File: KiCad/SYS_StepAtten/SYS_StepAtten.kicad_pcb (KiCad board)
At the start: 2 copper layers, 122 x 84 mm, 147 parts, among them J1 RCA-Out, J10 RCA1 GND JMP, J11 RCA2 GND JMP, J2 RCA-1, J3 RCA-2, J4 AUX-1-2, J5 Barrel_Jack 9Vac, J6 POT_EXT Conn, J7 cfg jumper, J8 ARM SWD, J9 A/D GND Jumper, K1 TQ2SA, K10 TQ2SA, K11 TQ2SA, K12 TQ2SA, K13 TQ2SA, K14 TQ2SA, K2 TQ2SA, K3 TQ2SA, K4 TQ2SA, K5 TQ2SA, K6 TQ2SA, K7 TQ2SA, K8 TQ2SA, K9 TQ2SA, Q1 2N7002, Q10 2N7002, Q11 2N7002, Q12 2N7002, Q13 2N7002, Q14 2N7002, Q2 2N7002, Q3 2N7002, Q4 2N7002, Q5 2N7002, Q6 2N7002, Q7 2N7002, Q8 2N7002, Q9 2N7002, SW1 INPUT_SWITCH, SW2 ON/OFF, U1 LM317, U2 L7805, U3 L7805, U4 STM32f030K6T6, Y1 8Mhz

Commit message: Base without relays
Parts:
- removed C6, C7: 22pf, Capacitor_SMD:C_0603_1608Metric
- removed Y1: 8Mhz, Crystal:Crystal_SMD_EuroQuartz_MJ-4Pin_5.0x3.2mm
- J10, J11: footprint Connector_PinSocket_2.54mm:PinSocket_1x03_P2.54mm_Vertical -> Connector_PinHeader_2.54mm:PinHeader_1x03_P2.54mm_Vertical
- moved Q14 440.9 mm to (642.0, -72.4)
- moved D23 424.9 mm to (647.1, -73.0), turned to 180 degrees
- moved Q13 416.0 mm to (624.2, -87.6)
- moved D22 402.5 mm to (629.2, -83.8), turned to 180 degrees
- moved Q12 358.2 mm to (561.3, -73.0)
- moved D21 340.3 mm to (566.4, -70.5)
- moved Q11 330.7 mm to (546.7, -73.7)
- moved D20 325.8 mm to (549.9, -64.1)
- moved Q10 297.6 mm to (518.8, -78.1)
- moved D19 289.7 mm to (517.5, -67.9)
- moved D1 254.2 mm to (45.7, 154.3), turned to 180 degrees
- moved D2 246.4 mm to (50.8, 154.3), turned to 0 degrees
- moved D8 245.6 mm to (45.9, 151.1), turned to 0 degrees
- moved D9 241.8 mm to (50.8, 151.1), turned to 180 degrees
- moved R31 234.2 mm to (31.8, 85.7), turned to 270 degrees
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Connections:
- K1 pad 2: /AUX1_GND -> Net-(K1-Pad2)
- K1 pad 4: /AUX2_GND -> Net-(K1-Pad4)
- K1 pad 7: Net-(K1-Pad7) -> /AUX2_GND
- K1 pad 9: Net-(K1-Pad9) -> /AUX1_GND
- K3 pad 4: Net-(K1-Pad3) -> Net-(K1-Pad8)
- K3 pad 7: Net-(K1-Pad3) -> Net-(K1-Pad8)
- U4 pad 2: /PF0_OSC -> Net-(U4-Pad2)
- U4 pad 3: /PF1_OSC -> Net-(U4-Pad3)
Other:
- board text added: "1 <- CFG1 -> 0"
- board text added: "1 <- CFG2 -> 0"
- board text added: "1 NO-YES"
- board text added: "2 NO-YES"
- board text added: "AGnd-DGnd:"
- board text added: "Below Line: Max Height -8mm"
- board text added: "L"
- board text added: "NO-YES"
- board text added: "ON/OFF"
- board text added: "Output Load Adj."
- board text added: "R"
- board text added: "Schilk's SYS Step Attenuator"
- board text added: "Short GndL & GndR:"
- board text added: "v0.1"

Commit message: Vertical
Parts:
- moved D8 137.7 mm to (179.1, 116.3), turned to 270 degrees
- moved D1 135.6 mm to (175.9, 116.2), turned to 90 degrees
- moved D9 131.7 mm to (179.1, 121.3), turned to 90 degrees
- moved D2 129.4 mm to (175.9, 121.3), turned to 270 degrees
- moved D15 116.1 mm to (153.0, 125.1), turned to 270 degrees
- moved R11 110.4 mm to (132.1, 139.1), turned to 270 degrees
- moved C11 110.1 mm to (178.4, 80.0), turned to 0 degrees
- moved U3 107.0 mm to (187.3, 78.7), turned to 270 degrees
- moved R9 106.0 mm to (132.1, 134.0), turned to 270 degrees
- moved HS2 104.9 mm to (192.4, 81.3), turned to 270 degrees
- moved F1 103.9 mm to (133.3, 83.8)
- moved K6 102.0 mm to (146.7, 116.8), turned to 90 degrees
- moved K7 100.4 mm to (123.8, 137.8), turned to 270 degrees
- moved R31 99.2 mm to (113.7, 141.6), turned to 90 degrees
- moved C4 98.1 mm to (178.4, 99.1), turned to 0 degrees
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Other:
- board text removed: "Schilk's SYS Step Attenuator"
- board text removed: "v0.1"

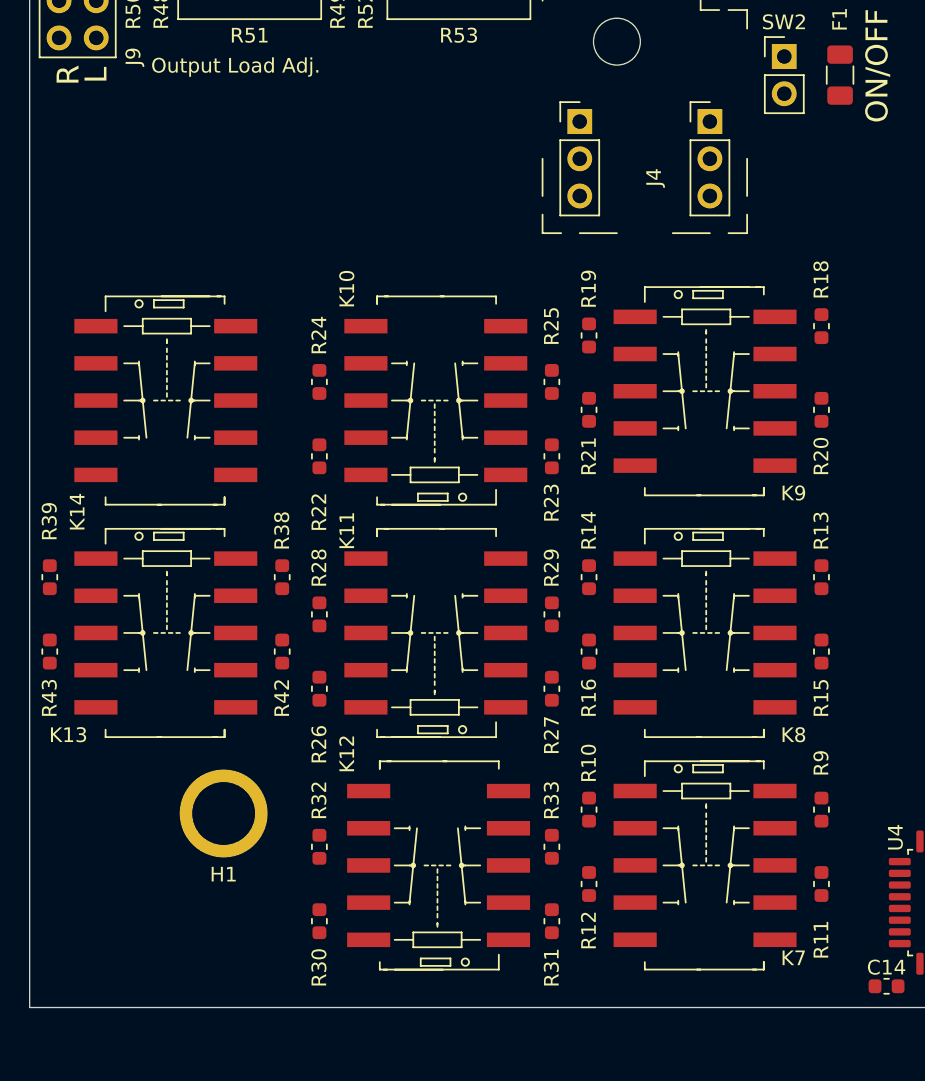
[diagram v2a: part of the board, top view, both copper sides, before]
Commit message: No 2nd Mounting Hole
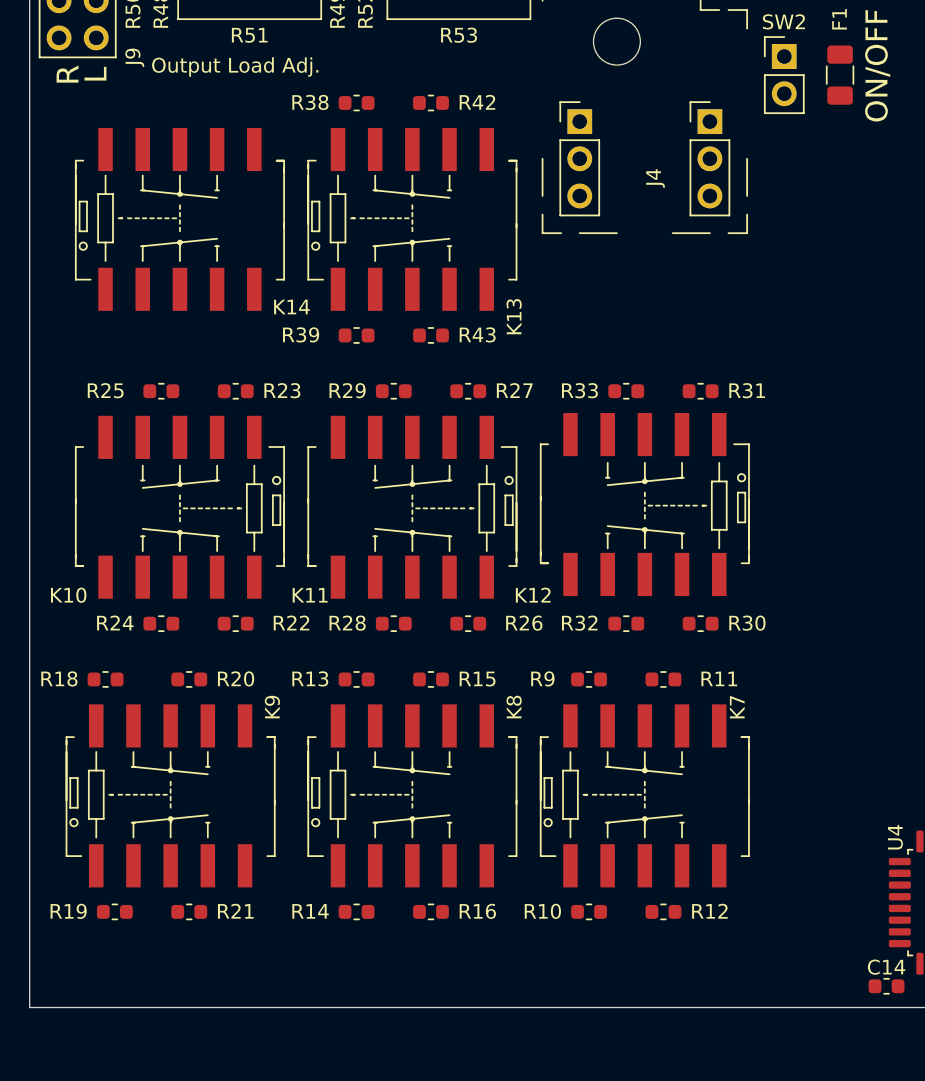
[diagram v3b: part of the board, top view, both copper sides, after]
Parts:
- removed H1: MountingHole 1, MountingHole_4.3mm_M4_ReducedSize:MountingHole_4.3mm_M4_Pad_Via
- moved R18 54.5 mm to (83.2, 125.1), turned to 0 degrees
- moved R19 51.0 mm to (83.8, 141.0), turned to 0 degrees
- moved R20 46.9 mm to (88.9, 125.1), turned to 0 degrees
- moved K9 45.7 mm to (87.6, 133.3), turned to 0 degrees
- moved R21 43.8 mm to (88.9, 141.0), turned to 0 degrees
- moved R42 38.8 mm to (105.4, 85.7), turned to 0 degrees
- moved R31 37.6 mm to (123.8, 105.4), turned to 180 degrees
- moved R43 33.8 mm to (105.4, 101.6), turned to 0 degrees
- moved R30 33.0 mm to (123.8, 121.3), turned to 180 degrees
- moved R38 32.8 mm to (100.3, 85.7), turned to 0 degrees
- moved K13 32.8 mm to (104.1, 94.0), turned to 0 degrees
- moved R13 32.5 mm to (100.3, 125.1), turned to 0 degrees
- moved R33 31.5 mm to (118.7, 105.4), turned to 180 degrees
- moved K12 28.5 mm to (120.0, 112.8), turned to 180 degrees
- moved R14 27.8 mm to (100.3, 141.0), turned to 0 degrees
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
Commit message: 1st Draft Parts Placement
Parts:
- moved Q14 599.7 mm to (83.2, 145.4), turned to 0 degrees
- moved D23 593.3 mm to (80.0, 101.6), turned to 90 degrees
- moved Q13 571.6 mm to (102.2, 145.4), turned to 0 degrees
- moved D22 563.7 mm to (96.4, 100.3)
- moved Q12 485.6 mm to (127.6, 145.4), turned to 0 degrees
- moved Q11 484.2 mm to (114.9, 145.4), turned to 0 degrees
- moved Q10 478.3 mm to (95.9, 145.4), turned to 0 degrees
- moved D21 472.1 mm to (130.2, 109.9), turned to 270 degrees
- moved D20 469.1 mm to (113.0, 106.7), turned to 0 degrees
- moved D19 455.8 mm to (96.5, 106.7), turned to 0 degrees
- moved D16 387.5 mm to (113.0, 139.7), turned to 180 degrees
- moved D17 372.1 mm to (96.5, 139.7), turned to 180 degrees
- moved Q8 369.3 mm to (108.6, 145.4), turned to 0 degrees
- moved Q7 353.8 mm to (121.3, 145.4), turned to 0 degrees
- moved R47 320.0 mm to (80.6, 145.4)
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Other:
- board text added: "1"
- board text added: "2"
- board text added: "LGND-RGND"
- board text removed: "1 NO-YES"
- board text removed: "2 NO-YES"
- board text removed: "Below Line: Max Height -8mm"
- board text removed: "Short GndL & GndR:"

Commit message: First Routing Draft
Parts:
- removed J11: RCA2 GND JMP, Connector_PinHeader_2.54mm:PinHeader_1x03_P2.54mm_Vertical
- C11, C3, C4, C8: footprint Capacitor_SMD:CP_Elec_8x6.9 -> Capacitor_Tantalum_SMD:CP_EIA-6032-20_AVX-F
- J10: value RCA1 GND JMP -> A/D GND Jumper; footprint Connector_PinHeader_2.54mm:PinHeader_1x03_P2.54mm_Vertical -> Connector_PinHeader_2.54mm:PinHeader_2x03_P2.54mm_Vertical
- moved HS2 103.9 mm to (88.9, 90.8), turned to 0 degrees
- moved U3 102.4 mm to (86.4, 95.9), turned to 0 degrees
- moved C11 91.7 mm to (88.9, 99.7), turned to 180 degrees
- moved HS1 87.9 mm to (104.8, 90.8), turned to 0 degrees
- moved U2 85.1 mm to (102.2, 95.9), turned to 0 degrees
- moved C12 80.2 mm to (94.0, 99.7), turned to 90 degrees
- moved C8 74.4 mm to (104.8, 99.7), turned to 180 degrees
- moved D8 67.7 mm to (118.7, 84.5)
- moved D1 67.6 mm to (115.6, 84.5)
- moved D2 67.6 mm to (115.6, 89.5)
- moved D9 67.6 mm to (118.7, 89.5)
- moved R37 64.1 mm to (142.9, 104.8), turned to 270 degrees
- moved Q10 64.1 mm to (145.4, 104.8)
- moved U1 63.9 mm to (130.0, 100.3), turned to 0 degrees
- moved C9 63.1 mm to (109.9, 99.7), turned to 90 degrees
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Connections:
- D16 pad 1: /+5V_A -> /+5V_B
- D20 pad 1: /+5V_B -> /+5V_A
- J10 pad 1: /RCA1_GNDR -> /RCA2_GNDR
- J10 pad 2: /RCA1_GNDL -> /RCA1_GNDR
- J10 pad 3: Net-(J10-Pad3) -> /RCA2_GNDL
- K11 pad 1: /+5V_B -> /+5V_A
- K7 pad 1: /+5V_A -> /+5V_B
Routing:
- net GND: track 0.00 -> 490.0 mm, vias 0 -> 24
- net /AGND_R: track 0.00 -> 383.4 mm, vias 0 -> 16
- net /+5V_B: track 0.00 -> 320.9 mm, vias 0 -> 15
- net /AGND_L: track 0.00 -> 282.4 mm, vias 0 -> 7
- net /+5V_A: track 0.00 -> 264.0 mm, vias 0 -> 19
- net +3V3: track 0.00 -> 221.2 mm, vias 0 -> 10
- net Net-(K6-Pad3): track 0.00 -> 207.4 mm, vias 0 -> 2
- net Net-(K6-Pad8): track 0.00 -> 194.5 mm, vias 0 -> 2
- net Net-(J6-Pad4): track 0.00 -> 185.9 mm, vias 0 -> 3
- net Net-(C2-Pad1): track 0.00 -> 172.9 mm, vias 0 -> 3
- net /rly_atten6: track 0.00 -> 154.0 mm, vias 0 -> 2
- net /rly_mute: track 0.00 -> 135.9 mm, vias 0 -> 2
- net /rly_atten0: track 0.00 -> 134.0 mm, vias 0 -> 2
- net /rly_atten5: track 0.00 -> 124.0 mm, vias 0 -> 2
- net /rly_atten1: track 0.00 -> 109.4 mm, vias 0 -> 2
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- added copper zone on B.Cu, net +3V3
- added copper zone on F.Cu, net /AGND_L
- added copper zone on F.Cu, net /AGND_R
- added copper zone on F.Cu, net GND
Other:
- board text added: "1 CFG1 0"
- board text added: "1 CFG2 0"
- board text removed: "1 <- CFG1 -> 0"
- board text removed: "1 <- CFG2 -> 0"

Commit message: Generated production files for v1.0
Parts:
- added REF**: KiCad-Logo2_8mm_SilkScreen, Symbol:KiCad-Logo2_8mm_SilkScreen, B.Cu at (89.2, 141.0)
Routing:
- net GND: track 490.0 -> 510.7 mm, vias 24 -> 28
- net +3V3: track 221.2 -> 221.8 mm
- net /NRST: track 79.9 -> 79.4 mm
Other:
- board text added: "SCHILK"
- board text added: "SYS - StepAtten [https://github.com/TheSchilk/SYS_StepAtten]"
- board text added: "v1.0"

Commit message: Small Fixes. Pfuh.
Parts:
- removed the REF** at (89.2, 141.0)
- added REF**: KiCad-Logo2_5mm_SilkScreen, Symbol:KiCad-Logo2_5mm_SilkScreen, F.Cu at (141.3, 93.3)
- moved D10 0.87 mm to (186.0, 144.4), turned to 90 degrees
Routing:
- net Net-(D10-Pad1): track 3.62 -> 8.78 mm, vias 0 -> 2
- net /+5V_A: track 264.0 -> 262.5 mm
- net /RCA2_GNDR: track 44.6 -> 46.0 mm, vias 3 -> 2
- net Net-(D10-Pad2): track 4.24 -> 5.52 mm
- net Net-(C2-Pad1): track 172.9 -> 174.1 mm
- net Net-(D10-Pad3): track 6.48 -> 5.58 mm
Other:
- board text added: "Ext. Pot."
- board text added: "OUT"
- board text added: "RCA1"
- board text added: "RCA2"

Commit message: Layout updated
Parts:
- removed C11: 100u, Capacitor_Tantalum_SMD:CP_EIA-6032-20_AVX-F
- removed C12, C9: 1uf, Capacitor_SMD:C_0603_1608Metric
- removed D2, D8, D9: 1N4001, Diode_SMD:D_SOD-123F
- removed HS1, HS2: Heatsink, XSD-C4649_TO220_Heatsink:XSD-C4649_TO220_Heatsink
- removed U3: L7805, Package_TO_SOT_THT:TO-220-3_Vertical
- added C6: 47pf, Capacitor_SMD:C_0603_1608Metric, F.Cu at (105.1, 97.2)
- added C7: 470u, Capacitor_SMD:CP_Elec_8x10.5, F.Cu at (91.1, 95.9)
- added G1: BarrelPolarity_CenterPos, BarrelPolarity_3mm:BarrelPolarity_3mm_CenterPos, B.Cu at (120.0, 67.3)
- added J11: ADJ_L, Connector_PinHeader_2.54mm:PinHeader_1x03_P2.54mm_Vertical, F.Cu at (92.4, 85.7)
- added J12: ADJ_R, Connector_PinHeader_2.54mm:PinHeader_1x03_P2.54mm_Vertical, F.Cu at (97.5, 85.7)
- added L1: 22uH/800mA, Inductor_SMD:L_Taiyo-Yuden_MD-4040, F.Cu at (98.7, 96.5)
- added R54: 0R33 / 0.5W min, Resistor_SMD:R_1210_3225Metric, F.Cu at (117.2, 95.2)
- added R55: 3K8, Resistor_SMD:R_0603_1608Metric, F.Cu at (108.3, 99.7)
- added R56: 1K2, Resistor_SMD:R_0603_1608Metric, F.Cu at (112.1, 99.7)
- C3: value 100u -> 1000u; footprint Capacitor_Tantalum_SMD:CP_EIA-6032-20_AVX-F -> Capacitor_SMD:CP_Elec_10x10.5
- C4, C8: value 100u -> 0u1; footprint Capacitor_Tantalum_SMD:CP_EIA-6032-20_AVX-F -> Capacitor_SMD:C_0603_1608Metric
- D1: value 1N4001 -> 1N5819
- D3, D4, D6, D7: value SD05T1G -> SD03
- J5: value Barrel_Jack 9Vac -> Barrel_Jack 9Vdc
- RV1: value VOL_POT -> 10K Linear
- U2: value L7805 -> MC34063AD; footprint Package_TO_SOT_THT:TO-220-3_Vertical -> Package_SO:SOIC-8_3.9x4.9mm_P1.27mm
- moved D1 17.7 mm to (102.6, 96.5), turned to 270 degrees
- moved C3 12.7 mm to (116.5, 87.0)
- moved C4 10.6 mm to (107.6, 90.8), turned to 270 degrees
- moved C8 9.23 mm to (98.7, 92.7), turned to 0 degrees
- moved U2 7.94 mm to (110.2, 95.9)
- moved F1 5.53 mm to (107.6, 85.6), turned to 90 degrees
- moved R49 0.95 mm to (101.9, 81.3)
- moved R52 0.95 mm to (98.1, 81.3)
- moved R50 0.32 mm to (87.9, 81.3)
- moved R48 0.32 mm to (91.8, 81.3)
- turned R1 to 90 degrees
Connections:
- C8 pad 1: /+5V_A -> +5V
- D1 pad 1: Net-(C3-Pad1) -> Net-(D1-Pad1)
- D1 pad 2: Net-(D1-Pad2) -> GND
- D11 pad 1: /+5V_A -> +5V
- D12 pad 1: /+5V_A -> +5V
- D13 pad 1: /+5V_A -> +5V
- D14 pad 1: /+5V_A -> +5V
- D15 pad 1: /+5V_A -> +5V
- D16 pad 1: /+5V_B -> +5V
- D17 pad 1: /+5V_B -> +5V
- D18 pad 1: /+5V_B -> +5V
- D19 pad 1: /+5V_B -> +5V
- D20 pad 1: /+5V_A -> +5V
- D21 pad 1: /+5V_B -> +5V
- D22 pad 1: /+5V_B -> +5V
- D23 pad 1: /+5V_B -> +5V
- D3 pad 2: /pot_ext_sense -> /extctrl_sense
- D4 pad 1: /pot_ext_sense -> /extctrl_sense
- D5 pad 1: /+5V_A -> +5V
- D6 pad 2: /pot_ext -> /extctrl_pot
- D7 pad 1: /pot_ext -> /extctrl_pot
- F1 pad 1: Net-(D1-Pad2) -> Net-(C3-Pad1)
- J10 pad 5: Net-(J10-Pad5) -> (no net)
- J10 pad 6: Net-(J10-Pad6) -> (no net)
- J5 pad 2: Net-(D2-Pad2) -> GND
- J8 pad 6: Net-(J8-Pad6) -> (no net)
- J8 pad 7: Net-(J8-Pad7) -> (no net)
- J8 pad 8: Net-(J8-Pad8) -> (no net)
- J8 pad 9: Net-(J8-Pad9) -> (no net)
- J9 pad 5: Net-(J9-Pad5) -> (no net)
- J9 pad 6: Net-(J9-Pad6) -> (no net)
- K1 pad 1: /+5V_A -> +5V
- K1 pad 2: Net-(K1-Pad2) -> (no net)
- K1 pad 3: Net-(K1-Pad3) -> (no net)
- K1 pad 4: Net-(K1-Pad4) -> (no net)
- K10 pad 1: /+5V_B -> +5V
- K11 pad 1: /+5V_A -> +5V
- K12 pad 1: /+5V_B -> +5V
- K13 pad 1: /+5V_B -> +5V
- K14 pad 1: /+5V_B -> +5V
- K2 pad 1: /+5V_A -> +5V
- K3 pad 1: /+5V_A -> +5V
- K4 pad 1: /+5V_A -> +5V
- K5 pad 1: /+5V_A -> +5V
- K6 pad 1: /+5V_A -> +5V
- K7 pad 1: /+5V_B -> +5V
- K8 pad 1: /+5V_B -> +5V
- K9 pad 1: /+5V_B -> +5V
- R1 pad 1: Net-(J6-Pad4) -> +3V3
- R1 pad 2: GND -> Net-(J6-Pad4)
- R2 pad 1: /pot_ext_sense -> /extctrl_sense
- R3 pad 1: /pot_ext -> /extctrl_pot
- R50 pad 1: Net-(J1-Pad2) -> Net-(J11-Pad3)
- R52 pad 1: Net-(J1-Pad4) -> Net-(J12-Pad1)
- SW1 pad 1: Net-(SW1-Pad1) -> (no net)
- SW1 pad 2: Net-(SW1-Pad2) -> (no net)
- SW1 pad 3: Net-(SW1-Pad3) -> (no net)
- SW1 pad 4: +3V3 -> GND
- SW1 pad 6: GND -> +3V3
- U2 pad 1: Net-(C3-Pad1) -> Net-(R54-Pad1)
- U2 pad 2: GND -> Net-(D1-Pad1)
- U2 pad 3: /+5V_A -> Net-(C6-Pad1)
- U4 pad 13: /led0 -> /extctrl_sense
- U4 pad 14: /pot_ext -> /led0
- U4 pad 2: Net-(U4-Pad2) -> (no net)
- U4 pad 20: Net-(U4-Pad20) -> (no net)
- U4 pad 27: /pot_ext_sense -> /extctrl_pot
- U4 pad 3: Net-(U4-Pad3) -> (no net)
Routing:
- net +5V: track 0.00 -> 600.7 mm, vias 0 -> 37
- net /+5V_B: track 320.9 -> 0.00 mm, vias 15 -> 0
- net /+5V_A: track 262.5 -> 0.00 mm, vias 19 -> 0
- net Net-(D2-Pad2): track 29.0 -> 0.00 mm
- net Net-(C3-Pad1): track 64.9 -> 39.1 mm
- net /extctrl_pot: track 0.00 -> 21.5 mm, vias 0 -> 2
- net /pot_ext_sense: track 19.4 -> 0.00 mm, vias 2 -> 0
- net GND: track 510.7 -> 529.8 mm, vias 28 -> 32
- net /rly_atten2: track 51.4 -> 32.9 mm, vias 4 -> 2
- net /pot_ext: track 11.4 -> 0.00 mm
- net /extctrl_sense: track 0.00 -> 11.2 mm
- net +3V3: track 222.3 -> 211.2 mm, vias 10 -> 14
- net Net-(R54-Pad1): track 0.00 -> 9.33 mm
- net Net-(D1-Pad1): track 0.00 -> 9.01 mm
- net /AGND_L: track 282.5 -> 289.1 mm
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- added copper zone on B.Cu, net GND
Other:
- board text added: "OFF-ON"
- board text added: "RCA LGND-RGND"
- board text added: "SYS StepAtten"
- board text added: "[https://github.com/TheSchilk/SYS_StepAtten]"
- board text added: "v1.1"
- board text removed: "LGND-RGND"
- board text removed: "SYS - StepAtten [https://github.com/TheSchilk/SYS_StepAtten]"
- board text removed: "v1.0"
